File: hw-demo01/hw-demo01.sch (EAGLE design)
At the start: 24 parts, among them IC3 MCP2562T, IC4 STM32F042, Q1 BTS50010

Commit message: fine tune layout, add voltage regulators
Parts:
- removed C5V1: 1u, rcl:C-USC0603K
- added C3VIN, C3VOUT, C5VIN, C5VOUT: 1u, rcl:C-USC0603K
- added TERM: 22-23-2021, con-molex:22-23-2021
- added VR3V3, VR5V0: (no value), SparkFun-PowerIC:V_REG_LM1117SOT223
- RTERM: device rcl:R-US_R0805 -> rcl:R-US_0204/7
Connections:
- removed net N$9: C5V1.2, RDIV2.1
- new net N$1: RTERM.1, TERM-1.S
- net +12V: now also C5VIN.1, VR5V0.IN; no longer C5V1.1
- net +3V3: now also C3VOUT.1, VR3V3.OUT, VR3V3.OUT@1
- net +5V: now also C3VIN.1, C5VOUT.1, VR3V3.IN, VR5V0.OUT, VR5V0.OUT@1
- net CANL: now also TERM-2.S; no longer RTERM.1
- net GND: now also C3VIN.2, C3VOUT.2, C5VIN.2, C5VOUT.2, RDIV2.1, VR3V3.ADJ, VR5V0.ADJ
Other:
- moved on the sheet: RDIV1, RDIV2

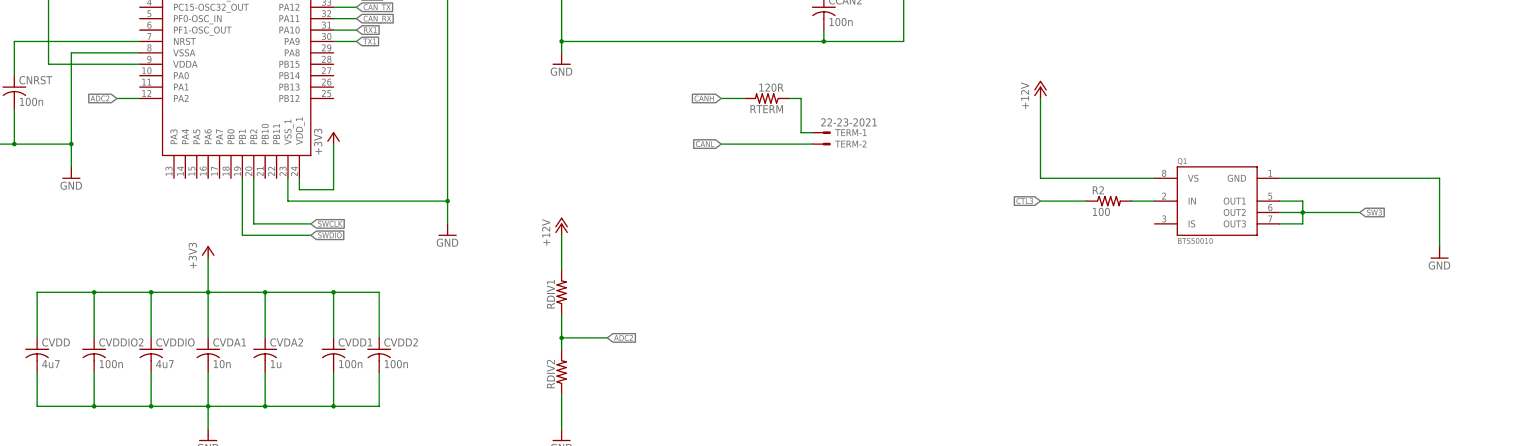
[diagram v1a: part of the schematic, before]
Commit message: Added test points, current monitoring and a few layout refinements
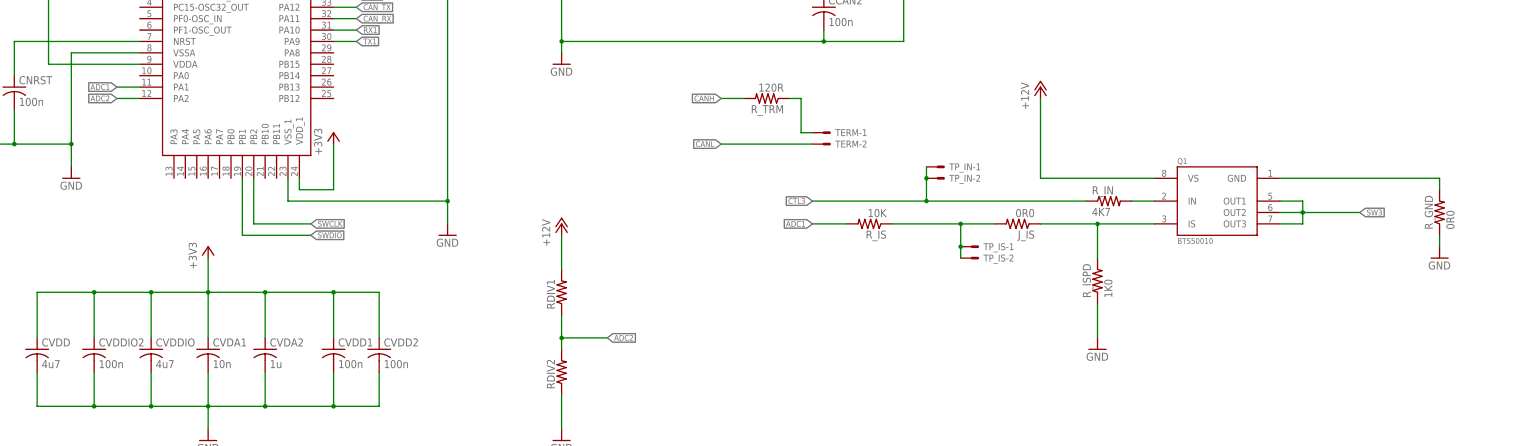
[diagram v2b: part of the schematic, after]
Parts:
- added J_IS: 0R0, rcl:R-US_0207/12
- added R_GND: 0R0, rcl:R-US_R1206W
- added R_IS: 10K, rcl:R-US_0207/12
- added R_ISPD: 1K0, rcl:R-US_0207/12
- added TP_IN, TP_IS: 22-23-2021, con-molex:22-23-2021
- R_IN: value 100 -> 4K7
- renumbered R2 to R_IN, RTERM to R_TRM
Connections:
- new net ADC1: IC4.PA1, R_IS.2
- new net IS: J_IS.1, Q1.IS, R_ISPD.2
- new net N$2: J_IS.2, R_IS.1, TP_IS-1.S, TP_IS-2.S
- new net N$3: Q1.GND, R_GND.2
- net CTL3: now also TP_IN-1.S, TP_IN-2.S
- net GND: now also R_GND.1, R_ISPD.1; no longer Q1.GND
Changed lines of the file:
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@@
 <part name="RDIV2" library="rcl" deviceset="R-US_" device="R0805"/>
 <part name="RBOOT0" library="rcl" deviceset="R-US_" device="R0603" value="100K"/>
-<part name="RTERM" library="rcl" deviceset="R-US_" device="0204/7" value="120R"/>
+<part name="R_TRM" library="rcl" deviceset="R-US_" device="0204/7" value="120R"/>
 <part name="FRAME1" library="frames" deviceset="FRAME_B_L" device=""/>
 <part name="Q1" library="BTS50010-1TAD" deviceset="BTS50010-1TAD" device="" value="BTS50010"/>
 <part name="P+1" library="supply1" deviceset="+12V" device=""/>
 <part name="GND3" library="supply1" deviceset="GND" device=""/>
-<part name="R2" library="rcl" deviceset="R-US_" device="0207/12" value="100"/>
+<part name="R_IN" library="rcl" deviceset="R-US_" device="0207/12" value="4K7"/>
 <part name="+12V" library="VP0265840000G" deviceset="VP0265840000G" device="" value=""/>
 <part name="LOAD+" library="VP0265840000G" deviceset="VP0265840000G" device="" value=""/>
@@
 <part name="GND4" library="supply1" deviceset="GND" device=""/>
 <part name="P+2" library="supply1" deviceset="+12V" device=""/>
-<part name="TERM" library="con-molex" deviceset="22-23-2021" device=""/>
+<part name="TERM" library="con-molex" deviceset="22-23-2021" device="" value=""/>
 <part name="VR5V0" library="SparkFun-PowerIC" deviceset="V_REG_LM1117" device="SOT223"/>
 <part name="P+3" library="supply1" deviceset="+12V" device=""/>
@@
 <part name="C3VOUT" library="rcl" deviceset="C-US" device="C0603K" value="1u"/>
 <part name="GND9" library="supply1" deviceset="GND" device=""/>
+<part name="R_ISPD" library="rcl" deviceset="R-US_" device="0207/12" value="1K0"/>
+<part name="GND14" library="supply1" deviceset="GND" device=""/>
+<part name="J_IS" library="rcl" deviceset="R-US_" device="0207/12" value="0R0"/>
+<part name="TP_IS" library="con-molex" deviceset="22-23-2021" device="" value=""/>
+<part name="TP_IN" library="con-molex" deviceset="22-23-2021" device="" value=""/>
+<part name="R_GND" library="rcl" deviceset="R-US_" device="R1206W" value="0R0"/>
+<part name="R_IS" library="rcl" deviceset="R-US_" device="0207/12" value="10K"/>
 </parts>
 <sheets>
@@
 <instance part="RDIV2" gate="G$1" x="76.2" y="121.92" rot="R90"/>
 <instance part="RBOOT0" gate="G$1" x="-50.8" y="223.52" rot="R90"/>
-<instance part="RTERM" gate="G$1" x="121.92" y="182.88" rot="R180"/>
+<instance part="R_TRM" gate="G$1" x="121.92" y="182.88" rot="R180"/>
 <instance part="FRAME1" gate="G$1" x="-111.76" y="0"/>
 <instance part="FRAME1" gate="G$2" x="213.36" y="0"/>
@@
 <instance part="P+1" gate="1" x="182.88" y="185.42"/>
 <instance part="GND3" gate="1" x="271.78" y="147.32"/>
-<instance part="R2" gate="G$1" x="198.12" y="160.02"/>
+<instance part="R_IN" gate="G$1" x="198.12" y="160.02"/>
 <instance part="+12V" gate="G$1" x="101.6" y="76.2"/>
 <instance part="LOAD+" gate="G$1" x="137.16" y="76.2" rot="MR180"/>
@@
 <instance part="C3VOUT" gate="G$1" x="2.54" y="40.64"/>
 <instance part="GND9" gate="1" x="76.2" y="106.68"/>
+<instance part="R_ISPD" gate="G$1" x="195.58" y="142.24" rot="R90"/>
+<instance part="GND14" gate="1" x="195.58" y="127"/>
+<instance part="J_IS" gate="G$1" x="177.8" y="154.94" rot="R180"/>
+<instance part="TP_IS" gate="-1" x="167.64" y="149.86"/>
+<instance part="TP_IS" gate="-2" x="167.64" y="147.32"/>
+<instance part="TP_IN" gate="-1" x="160.02" y="167.64"/>
+<instance part="TP_IN" gate="-2" x="160.02" y="165.1"/>
+<instance part="R_GND" gate="G$1" x="271.78" y="157.48" rot="R90"/>
+<instance part="R_IS" gate="G$1" x="144.78" y="154.94" rot="R180"/>
 </instances>
 <busses>
@@
 </segment>
 <segment>
-<pinref part="Q1" gate="G1" pin="GND"/>
-<pinref part="GND3" gate="1" pin="GND"/>
-<wire x1="236.22" y1="165.1" x2="271.78" y2="165.1" width="0.1524" layer="91"/>
-<wire x1="271.78" y1="165.1" x2="271.78" y2="149.86" width="0.1524" layer="91"/>
-</segment>
-<segment>
 <pinref part="+12V" gate="G$1" pin="2_2"/>
 <wire x1="91.44" y1="71.12" x2="86.36" y2="71.12" width="0.1524" layer="91"/>
@@
 <pinref part="GND9" gate="1" pin="GND"/>
 </segment>
+<segment>
+<pinref part="GND14" gate="1" pin="GND"/>
+<pinref part="R_ISPD" gate="G$1" pin="1"/>
+<wire x1="195.58" y1="129.54" x2="195.58" y2="137.16" width="0.1524" layer="91"/>
+</segment>
+<segment>
+<pinref part="GND3" gate="1" pin="GND"/>
+<pinref part="R_GND" gate="G$1" pin="1"/>
+<wire x1="271.78" y1="149.86" x2="271.78" y2="152.4" width="0.1524" layer="91"/>
+</segment>
 </net>
 <net name="CANH" class="0">
@@
 </segment>
 <segment>
-<pinref part="RTERM" gate="G$1" pin="2"/>
+<pinref part="R_TRM" gate="G$1" pin="2"/>
 <wire x1="111.76" y1="182.88" x2="116.84" y2="182.88" width="0.1524" layer="91"/>
 <label x="111.76" y="182.88" size="1.27" layer="95" rot="R180" xref="yes"/>
@@
 </segment>
 <segment>
-<pinref part="R2" gate="G$1" pin="1"/>
-<wire x1="182.88" y1="160.02" x2="193.04" y2="160.02" width="0.1524" layer="91"/>
-<label x="182.88" y="160.02" size="1.27" layer="95" rot="R180" xref="yes"/>
+<pinref part="R_IN" gate="G$1" pin="1"/>
+<wire x1="132.08" y1="160.02" x2="157.48" y2="160.02" width="0.1524" layer="91"/>
+<label x="132.08" y="160.02" size="1.27" layer="95" rot="R180" xref="yes"/>
+<pinref part="TP_IN" gate="-1" pin="S"/>
+<pinref part="TP_IN" gate="-2" pin="S"/>
+<wire x1="157.48" y1="160.02" x2="193.04" y2="160.02" width="0.1524" layer="91"/>
+<wire x1="157.48" y1="167.64" x2="157.48" y2="165.1" width="0.1524" layer="91"/>
+<wire x1="157.48" y1="165.1" x2="157.48" y2="160.02" width="0.1524" layer="91"/>
+<junction x="157.48" y="165.1"/>
+<junction x="157.48" y="160.02"/>
 </segment>
 </net>
@@
 <segment>
 <pinref part="Q1" gate="G1" pin="IN"/>
-<pinref part="R2" gate="G$1" pin="2"/>
+<pinref part="R_IN" gate="G$1" pin="2"/>
 <wire x1="203.2" y1="160.02" x2="208.28" y2="160.02" width="0.1524" layer="91"/>
 </segment>
@@
 <net name="N$1" class="0">
 <segment>
-<pinref part="RTERM" gate="G$1" pin="1"/>
+<pinref part="R_TRM" gate="G$1" pin="1"/>
 <wire x1="127" y1="182.88" x2="129.54" y2="182.88" width="0.1524" layer="91"/>
 <wire x1="129.54" y1="182.88" x2="129.54" y2="175.26" width="0.1524" layer="91"/>
@@
 </segment>
 </net>
+<net name="IS" class="0">
+<segment>
+<pinref part="Q1" gate="G1" pin="IS"/>
+<pinref part="R_ISPD" gate="G$1" pin="2"/>
+<wire x1="208.28" y1="154.94" x2="195.58" y2="154.94" width="0.1524" layer="91"/>
+<wire x1="195.58" y1="154.94" x2="195.58" y2="147.32" width="0.1524" layer="91"/>
+<wire x1="195.58" y1="154.94" x2="182.88" y2="154.94" width="0.1524" layer="91"/>
+<junction x="195.58" y="154.94"/>
+<pinref part="J_IS" gate="G$1" pin="1"/>
+</segment>
+</net>
+<net name="ADC1" class="0">
+<segment>
+<pinref part="IC4" gate="G$1" pin="PA1"/>
+<wire x1="-22.86" y1="185.42" x2="-17.78" y2="185.42" width="0.1524" layer="91"/>
+<label x="-22.86" y="185.42" size="1.27" layer="95" rot="R180" xref="yes"/>
+</segment>
+<segment>
+<label x="132.08" y="154.94" size="1.27" layer="95" rot="R180" xref="yes"/>
+<pinref part="R_IS" gate="G$1" pin="2"/>
+<wire x1="139.7" y1="154.94" x2="132.08" y2="154.94" width="0.1524" layer="91"/>
+</segment>
+</net>
+<net name="N$3" class="0">
+<segment>
+<pinref part="Q1" gate="G1" pin="GND"/>
+<wire x1="236.22" y1="165.1" x2="271.78" y2="165.1" width="0.1524" layer="91"/>
+<pinref part="R_GND" gate="G$1" pin="2"/>
+<wire x1="271.78" y1="162.56" x2="271.78" y2="165.1" width="0.1524" layer="91"/>
+</segment>
+</net>
+<net name="N$2" class="0">
+<segment>
+<pinref part="TP_IS" gate="-2" pin="S"/>
+<pinref part="TP_IS" gate="-1" pin="S"/>
+<wire x1="165.1" y1="149.86" x2="165.1" y2="147.32" width="0.1524" layer="91"/>
+<pinref part="R_IS" gate="G$1" pin="1"/>
+<pinref part="J_IS" gate="G$1" pin="2"/>
+<wire x1="149.86" y1="154.94" x2="165.1" y2="154.94" width="0.1524" layer="91"/>
+<wire x1="165.1" y1="154.94" x2="172.72" y2="154.94" width="0.1524" layer="91"/>
+<wire x1="165.1" y1="149.86" x2="165.1" y2="154.94" width="0.1524" layer="91"/>
+<junction x="165.1" y="149.86"/>
+<junction x="165.1" y="154.94"/>
+</segment>
+</net>

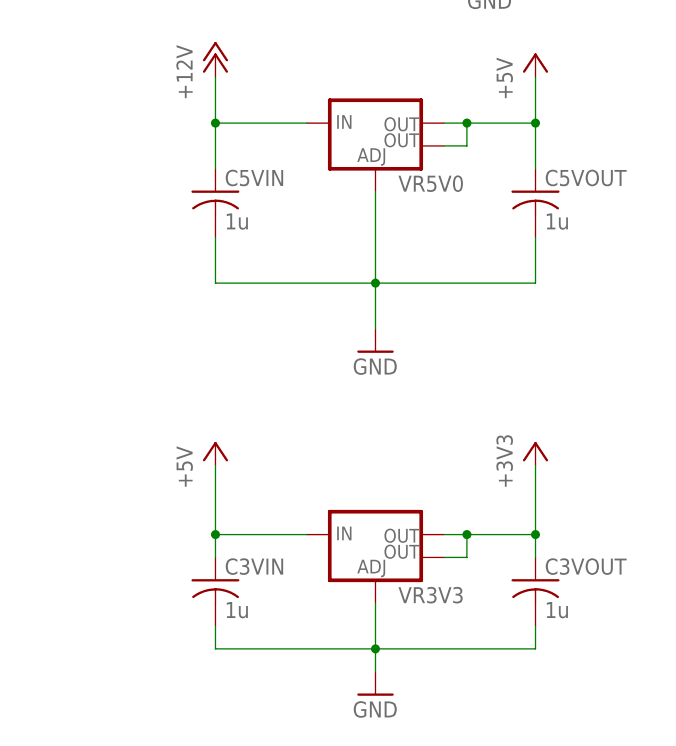
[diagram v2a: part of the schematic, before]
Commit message: Fix some capacitor packages and DRC errors
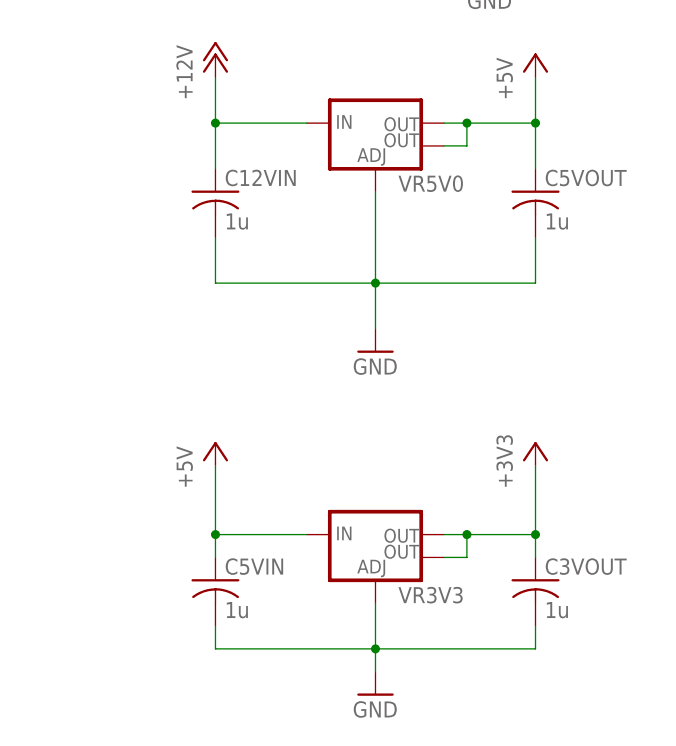
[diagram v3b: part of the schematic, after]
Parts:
- removed C3VIN: 1u, rcl:C-USC0603K
- added C12VIN: 1u, rcl:C-USC1206K
- C3VOUT, C5VOUT: device rcl:C-USC0603K -> rcl:C-USC0805K
- C5VIN: device rcl:C-USC0603K -> rcl:C-USC1206K
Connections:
- net +12V: now also C12VIN.1; no longer C5VIN.1
- net +5V: now also C5VIN.1; no longer C3VIN.1
- net GND: now also C12VIN.2; no longer C3VIN.2
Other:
- moved on the sheet: C5VIN
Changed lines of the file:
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@@
 <part name="P+7" library="supply1" deviceset="+5V" device=""/>
 <part name="+3V1" library="supply1" deviceset="+3V3" device=""/>
-<part name="C5VIN" library="rcl" deviceset="C-US" device="C0603K" value="1u"/>
-<part name="C5VOUT" library="rcl" deviceset="C-US" device="C0603K" value="1u"/>
+<part name="C12VIN" library="rcl" deviceset="C-US" device="C1206K" value="1u"/>
+<part name="C5VOUT" library="rcl" deviceset="C-US" device="C0805K" value="1u"/>
 <part name="GND7" library="supply1" deviceset="GND" device=""/>
 <part name="GND8" library="supply1" deviceset="GND" device=""/>
-<part name="C3VIN" library="rcl" deviceset="C-US" device="C0603K" value="1u"/>
-<part name="C3VOUT" library="rcl" deviceset="C-US" device="C0603K" value="1u"/>
+<part name="C5VIN" library="rcl" deviceset="C-US" device="C1206K" value="1u"/>
+<part name="C3VOUT" library="rcl" deviceset="C-US" device="C0805K" value="1u"/>
 <part name="GND9" library="supply1" deviceset="GND" device=""/>
 <part name="R_ISPD" library="rcl" deviceset="R-US_" device="0207/12" value="1K0"/>
@@
 <instance part="P+7" gate="1" x="-33.02" y="55.88"/>
 <instance part="+3V1" gate="G$1" x="2.54" y="55.88"/>
-<instance part="C5VIN" gate="G$1" x="-33.02" y="83.82"/>
+<instance part="C12VIN" gate="G$1" x="-33.02" y="83.82"/>
 <instance part="C5VOUT" gate="G$1" x="2.54" y="83.82"/>
 <instance part="GND7" gate="1" x="-15.24" y="66.04"/>
 <instance part="GND8" gate="1" x="-15.24" y="27.94"/>
-<instance part="C3VIN" gate="G$1" x="-33.02" y="40.64"/>
+<instance part="C5VIN" gate="G$1" x="-33.02" y="40.64"/>
 <instance part="C3VOUT" gate="G$1" x="2.54" y="40.64"/>
 <instance part="GND9" gate="1" x="76.2" y="106.68"/>
@@
 </segment>
 <segment>
-<pinref part="C5VIN" gate="G$1" pin="2"/>
+<pinref part="C12VIN" gate="G$1" pin="2"/>
 <wire x1="-33.02" y1="78.74" x2="-33.02" y2="73.66" width="0.1524" layer="91"/>
 <pinref part="GND7" gate="1" pin="GND"/>
@@
 </segment>
 <segment>
-<pinref part="C3VIN" gate="G$1" pin="2"/>
+<pinref part="C5VIN" gate="G$1" pin="2"/>
 <wire x1="-33.02" y1="35.56" x2="-33.02" y2="33.02" width="0.1524" layer="91"/>
 <pinref part="GND8" gate="1" pin="GND"/>
@@
 <wire x1="-22.86" y1="91.44" x2="-33.02" y2="91.44" width="0.1524" layer="91"/>
 <wire x1="-33.02" y1="91.44" x2="-33.02" y2="96.52" width="0.1524" layer="91"/>
-<pinref part="C5VIN" gate="G$1" pin="1"/>
+<pinref part="C12VIN" gate="G$1" pin="1"/>
 <wire x1="-33.02" y1="86.36" x2="-33.02" y2="91.44" width="0.1524" layer="91"/>
 <junction x="-33.02" y="91.44"/>
@@
 </segment>
 <segment>
-<pinref part="C3VIN" gate="G$1" pin="1"/>
+<pinref part="C5VIN" gate="G$1" pin="1"/>
 <pinref part="P+7" gate="1" pin="+5V"/>
 <wire x1="-33.02" y1="43.18" x2="-33.02" y2="45.72" width="0.1524" layer="91"/>

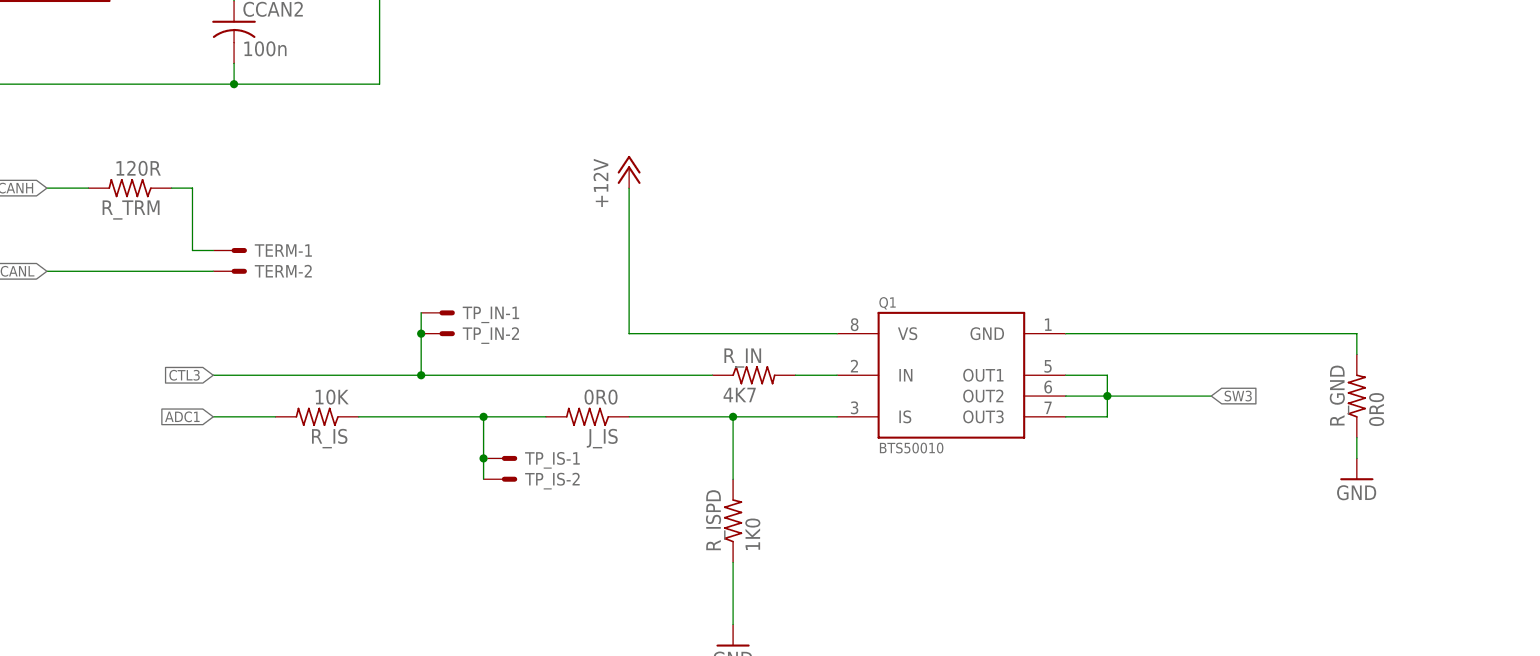
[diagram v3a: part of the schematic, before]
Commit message: fixed board footprint for smart switch, added recommended Vs capacitor
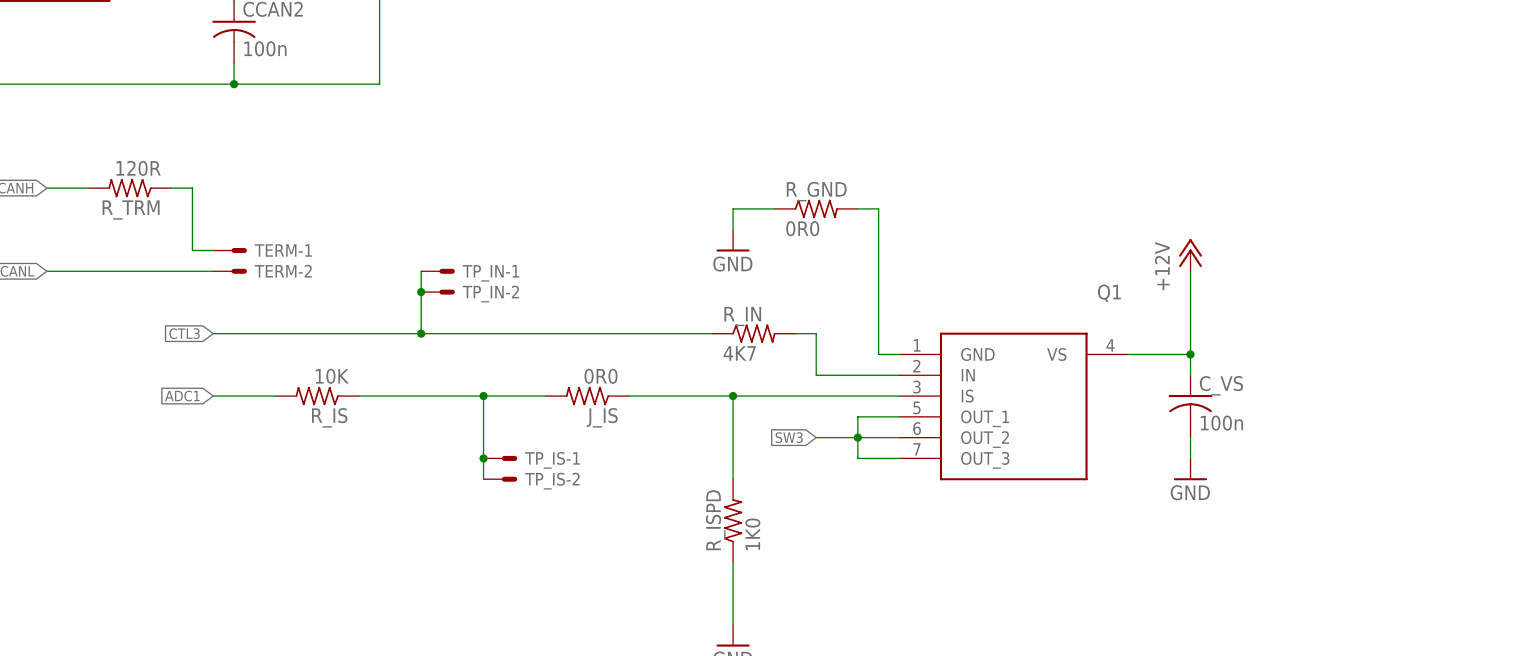
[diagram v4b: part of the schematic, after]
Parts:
- added C_VS: 100n, rcl:C-USC0603K
- Q1: value BTS50010 -> BTS500101TADATMA2; device BTS50010-1TAD:BTS50010-1TAD -> BTS500101TADATMA2:BTS500101TADATMA2
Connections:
- net +12V: now also C_VS.1
- net GND: now also C_VS.2
- net SW3: now also Q1.OUT_1, Q1.OUT_2, Q1.OUT_3; no longer Q1.OUT1, Q1.OUT2, Q1.OUT3
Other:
- moved on the sheet: J_IS, R_GND, R_IN, R_IS, TP_IN-1, TP_IN-2
